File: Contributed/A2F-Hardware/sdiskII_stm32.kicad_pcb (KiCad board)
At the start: 2 copper layers, 71.1 x 124.5 mm, 59 parts, among them J1 SDISKII IN (CARD), J2 SDISKII OUT (DRIVE), J3 EA W128064-OLED (FPC31), J4 UART, U1 BlackPill STMF4X1, U2 DM-OLED096-636, U3 EA OLEDM128-6, U4 74x257

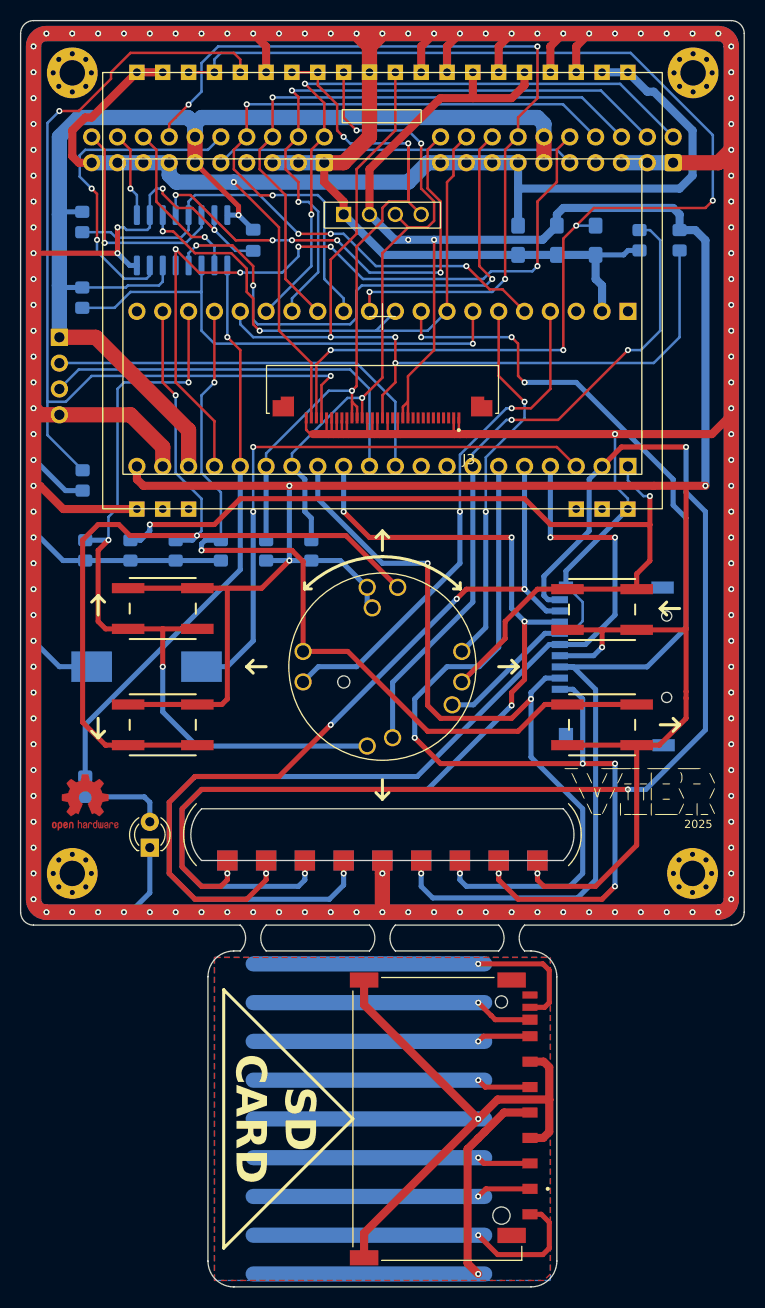
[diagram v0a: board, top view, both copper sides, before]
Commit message: Initial upload
Rotary encoder support buggy
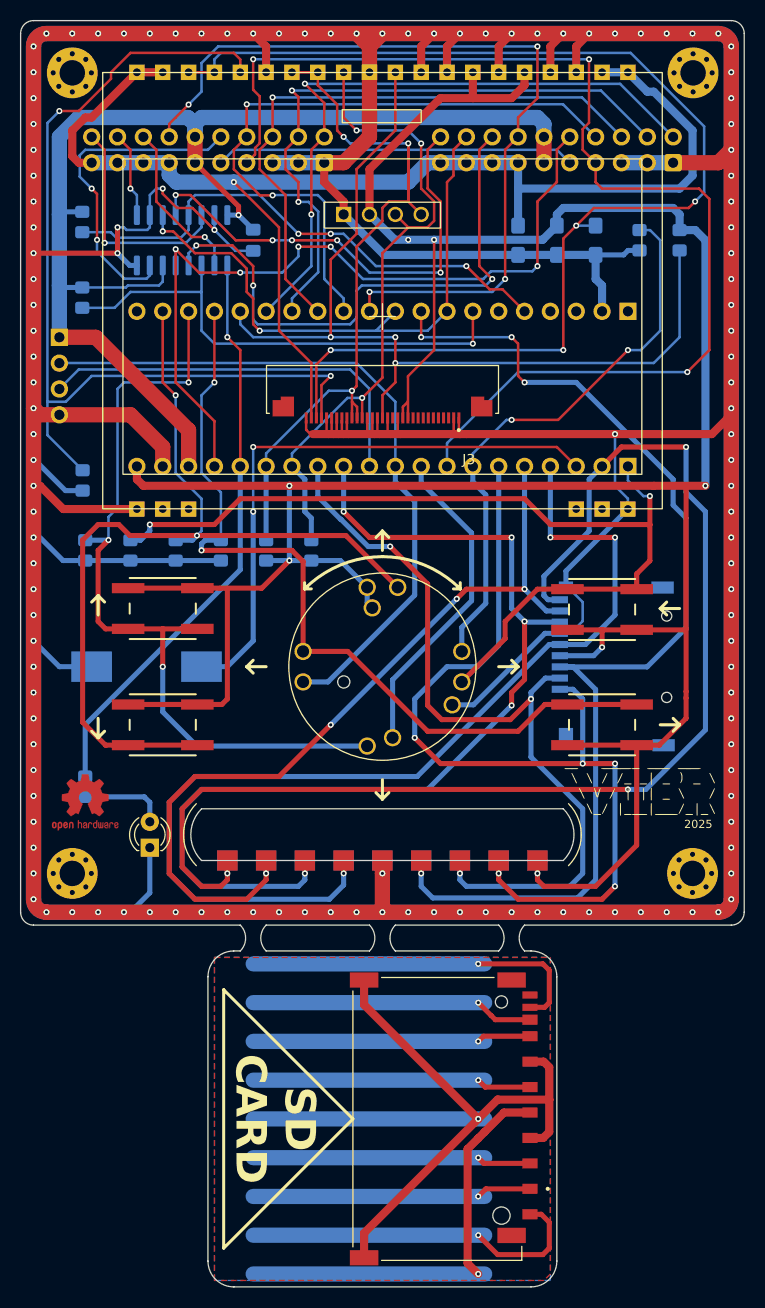
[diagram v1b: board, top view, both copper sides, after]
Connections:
- J1 pad 7: unconnected-(J1-Pin_7-Pad7) -> 3.5DSK
- J2 pad 7: unconnected-(J2-Pin_7-Pad7) -> 3.5DSK
- S5 pad EN_A: TIM2_CH3 -> USART1_TX
- S5 pad EN_B: TIM3_CH4 -> DEBUG
- S5 pad P: DEBUG -> USB_P
- U1 pad 8: unconnected-(U1-A11-Pad8) -> 3.5DSK
- U1 pad 9: unconnected-(U1-A12-Pad9) -> USB_P
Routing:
- net 3.5DSK: track 0.00 -> 115.4 mm, vias 0 -> 3
- net TIM2_CH3: track 50.1 -> 0.00 mm, vias 2 -> 0
- net TIM3_CH4: track 37.0 -> 0.00 mm, vias 2 -> 0
- net USB_P: track 0.00 -> 31.9 mm
- net USART1_TX: track 40.9 -> 68.9 mm
- net DEBUG: track 66.0 -> 55.7 mm
- net VCOMH: track 122.4 -> 120.7 mm
- net SDIO_D3: track 109.5 -> 108.3 mm

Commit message: RE update
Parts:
- added R13: 10K, Resistor_SMD:R_0805_2012Metric_Pad1.20x1.40mm_HandSolder, B.Cu at (151.1, 104.1)
- LS1: value BUZZER CT-1205H-SMT -> CT-1205H-SMT
- moved R12 35.5 mm to (146.7, 104.1)
- moved R2 4.19 mm to (164.7, 73.7)
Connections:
- R12 pad 1: DEBUG -> PA13
- S5 pad EN_A: USART1_TX -> PA13
- S5 pad EN_B: DEBUG -> PA14
- S5 pad P: USB_P -> unconnected-(S5A-PUSH-PadP)
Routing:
- net PA13: track 0.00 -> 57.3 mm, vias 0 -> 3
- net PA14: track 0.00 -> 56.5 mm, vias 0 -> 4
- net DEBUG: track 55.7 -> 0.00 mm, vias 2 -> 0
- net USB_P: track 31.9 -> 0.00 mm
- net USART1_TX: track 68.9 -> 44.1 mm
- net GND: track 425.7 -> 437.7 mm, vias 129 -> 131
- net BTN_DOWN: track 90.4 -> 97.0 mm
- net IREF: track 93.0 -> 97.7 mm
- net USART1_RX: track 39.7 -> 43.8 mm
- net BTN_UP: track 79.9 -> 82.7 mm
- net /RES: track 92.0 -> 89.5 mm
- net SDIO_D1: track 110.1 -> 111.9 mm
- net SDIO_D3: track 108.3 -> 109.9 mm
- net I2C_SCL: track 65.9 -> 67.3 mm
- net SDIO_D2: track 125.1 -> 126.3 mm
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
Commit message: Make Filsystem fixed
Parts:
- U1: footprint acheron_Hardware.pretty-master:Mini_F4X1_STM32_VIB -> sdisk_stm32:Mini_F4X1_STM32_VIB
- moved J4 1.27 mm to (108.0, 84.5)
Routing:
- net USART1_TX: track 44.1 -> 46.6 mm
- net USART1_RX: track 43.8 -> 46.0 mm
- net IREF: track 97.7 -> 99.3 mm
- net I2C_SCL: track 67.3 -> 68.3 mm
- net PA14: track 56.5 -> 55.7 mm, vias 4 -> 3
- net VCC: track 121.5 -> 120.8 mm
- net I2C_SDA: track 76.9 -> 77.5 mm
- net GND: track 437.7 -> 438.3 mm

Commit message: final v0.80.1
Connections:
- S5 pad P: unconnected-(S5A-PUSH-PadP) -> BTN_ENTR
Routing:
- net BTN_ENTR: track 82.4 -> 85.9 mm
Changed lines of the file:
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@@
 	(net 62 "unconnected-(U3-Pad3)")
 	(net 63 "unconnected-(SD2-WP-Pad11)")
-	(net 64 "unconnected-(S5A-PUSH-PadP)")
-	(net 65 "PA13")
-	(net 66 "PA14")
-	(net 67 "unconnected-(U1-3.3V-Pad41)")
-	(net 68 "unconnected-(U1-GND-Pad44)")
+	(net 64 "PA13")
+	(net 65 "PA14")
+	(net 66 "unconnected-(U1-3.3V-Pad41)")
+	(net 67 "unconnected-(U1-GND-Pad44)")
 	(footprint "sdisk_stm32:SD_CARD_AMPHENOL_GMC020080HR"
 		(layer "F.Cu")
@@
 			(layers "*.Cu" "*.Mask")
 			(remove_unused_layers no)
-			(net 65 "PA13")
+			(net 64 "PA13")
 			(pintype "passive")
 			(solder_mask_margin 0.102)
@@
 			(layers "*.Cu" "*.Mask")
 			(remove_unused_layers no)
-			(net 66 "PA14")
+			(net 65 "PA14")
 			(pintype "passive")
 			(solder_mask_margin 0.102)
@@
 			(layers "*.Cu" "*.Mask")
 			(remove_unused_layers no)
-			(net 64 "unconnected-(S5A-PUSH-PadP)")
+			(net 16 "BTN_ENTR")
 			(pinfunction "PUSH")
 			(pintype "passive")
@@
 			(layers "*.Cu" "*.Mask")
 			(remove_unused_layers no)
-			(net 67 "unconnected-(U1-3.3V-Pad41)")
+			(net 66 "unconnected-(U1-3.3V-Pad41)")
 			(pinfunction "3.3V")
 			(pintype "power_in+no_connect")
@@
 			(layers "*.Cu" "*.Mask")
 			(remove_unused_layers no)
-			(net 65 "PA13")
+			(net 64 "PA13")
 			(pinfunction "SDIO")
 			(pintype "bidirectional")
@@
 			(layers "*.Cu" "*.Mask")
 			(remove_unused_layers no)
-			(net 66 "PA14")
+			(net 65 "PA14")
 			(pinfunction "SCK")
 			(pintype "bidirectional")
@@
 			(layers "*.Cu" "*.Mask")
 			(remove_unused_layers no)
-			(net 68 "unconnected-(U1-GND-Pad44)")
+			(net 67 "unconnected-(U1-GND-Pad44)")
 			(pinfunction "GND")
 			(pintype "power_in+no_connect")
@@
 			(layers "B.Cu" "B.Mask" "B.Paste")
 			(roundrect_rratio 0.208333)
-			(net 65 "PA13")
+			(net 64 "PA13")
 			(pintype "passive")
 		)
@@
 			(layers "B.Cu" "B.Mask" "B.Paste")
 			(roundrect_rratio 0.208333)
-			(net 66 "PA14")
+			(net 65 "PA14")
 			(pintype "passive")
 		)
@@
 	)
 	(segment
-		(start 155.67 119.285)
-		(end 157.89 119.285)
+		(start 157.89 119.285)
+		(end 155.67 119.285)
 		(width 0.5)
 		(layer "F.Cu")
@@
 	)
 	(segment
-		(start 124.46 88.392)
-		(end 124.46 94.361)
-		(width 0.25)
+		(start 143.1102 120.142)
+		(end 143.129 120.142)
+		(width 0.5)
 		(layer "F.Cu")
 		(net 16)
 	)
 	(segment
-		(start 157.89 119.285)
-		(end 164.69 119.285)
+		(start 137.184 114.07)
+		(end 131.9022 114.07)
 		(width 0.5)
 		(layer "F.Cu")
@@
 	)
 	(segment
-		(start 131.9022 114.07)
-		(end 136.295 114.07)
+		(start 137.184 114.197)
+		(end 137.184 114.07)
 		(width 0.5)
 		(layer "F.Cu")
@@
 	)
 	(segment
-		(start 131.9022 105.2322)
-		(end 130.81 104.14)
+		(start 140.7022 122.55)
+		(end 143.1102 120.142)
 		(width 0.5)
 		(layer "F.Cu")
@@
 	)
 	(segment
-		(start 123.19 87.122)
-		(end 124.46 88.392)
+		(start 155.67 119.285)
+		(end 153.035 121.92)
+		(width 0.5)
+		(layer "F.Cu")
+		(net 16)
+	)
+	(segment
+		(start 124.46 88.392)
+		(end 124.46 94.361)
 		(width 0.25)
 		(layer "F.Cu")
@@
 	)
 	(segment
-		(start 136.295 114.07)
-		(end 144.145 121.92)
+		(start 143.129 120.142)
+		(end 137.184 114.197)
 		(width 0.5)
 		(layer "F.Cu")
@@
 	)
 	(segment
-		(start 144.145 121.92)
-		(end 153.035 121.92)
+		(start 157.89 119.285)
+		(end 164.69 119.285)
 		(width 0.5)
 		(layer "F.Cu")
@@
 	)
 	(segment
-		(start 153.035 121.92)
-		(end 155.67 119.285)
+		(start 131.9022 105.2322)
+		(end 130.81 104.14)
 		(width 0.5)
 		(layer "F.Cu")
@@
 	)
 	(segment
+		(start 123.19 87.122)
+		(end 124.46 88.392)
+		(width 0.25)
+		(layer "F.Cu")
+		(net 16)
+	)
+	(segment
 		(start 123.19 80.645)
 		(end 123.19 87.122)
@@
 	)
 	(segment
+		(start 144.907 121.92)
+		(end 143.129 120.142)
+		(width 0.5)
+		(layer "F.Cu")
+		(net 16)
+	)
+	(segment
 		(start 131.9022 114.07)
 		(end 131.9022 105.2322)
@@
 		(net 16)
 	)
+	(segment
+		(start 153.035 121.92)
+		(end 144.907 121.92)
+		(width 0.5)
+		(layer "F.Cu")
+		(net 16)
+	)
 	(via
 		(at 124.46 94.361)
@@
 		(width 0.25)
 		(layer "F.Cu")
-		(net 65)
+		(net 64)
 	)
 	(segment
@@
 		(width 0.25)
 		(layer "F.Cu")
-		(net 65)
+		(net 64)
 	)
 	(segment
@@
 		(width 0.25)
 		(layer "F.Cu")
-		(net 65)
+		(net 64)
 	)
 	(via
@@
 		(drill 0.3)
 		(layers "F.Cu" "B.Cu")
-		(net 65)
+		(net 64)
 	)
 	(via
@@
 		(drill 0.3)
 		(layers "F.Cu" "B.Cu")
-		(net 65)
+		(net 64)
 	)
 	(via
@@
 		(drill 0.3)
 		(layers "F.Cu" "B.Cu")
-		(net 65)
+		(net 64)
 	)
 	(segment
@@
 		(width 0.5)
 		(layer "B.Cu")
-		(net 65)
+		(net 64)
 	)
 	(segment
@@
 		(width 0.25)
 		(layer "B.Cu")
-		(net 65)
+		(net 64)
 	)
 	(segment
@@
 		(width 0.5)
 		(layer "B.Cu")
-		(net 65)
+		(net 64)
 	)
 	(segment
@@
 		(width 0.25)
 		(layer "B.Cu")
-		(net 65)
+		(net 64)
 	)
 	(segment
@@
 		(width 0.5)
 		(layer "B.Cu")
-		(net 65)
+		(net 64)
 	)
 	(segment
@@
 		(width 0.25)
 		(layer "B.Cu")
-		(net 65)
+		(net 64)
 	)
 	(segment
@@
 		(width 0.25)
 		(layer "B.Cu")
-		(net 65)
+		(net 64)
 	)
 	(segment
@@
 		(width 0.5)
 		(layer "B.Cu")
-		(net 65)
+		(net 64)
 	)
 	(segment
@@
 		(width 0.5)
 		(layer "B.Cu")
-		(net 65)
+		(net 64)
 	)
 	(segment
@@
 		(width 0.5)
 		(layer "B.Cu")
-		(net 65)
+		(net 64)
 	)
 	(segment
@@
 		(width 0.25)
 		(layer "B.Cu")
-		(net 65)
+		(net 64)
 	)
 	(segment
@@
 		(width 0.5)
 		(layer "B.Cu")
-		(net 65)
+		(net 64)
 	)
 	(segment
@@
 		(width 0.5)
 		(layer "B.Cu")
-		(net 65)
+		(net 64)
 	)
 	(segment
@@
 		(width 0.25)
 		(layer "F.Cu")
-		(net 66)
+		(net 65)
 	)
 	(segment
@@
 		(width 0.25)
 		(layer "F.Cu")
-		(net 66)
+		(net 65)
 	)
 	(segment
@@
 		(width 0.5)
 		(layer "F.Cu")
-		(net 66)
+		(net 65)
 	)
 	(segment
@@
 		(width 0.25)
 		(layer "F.Cu")
-		(net 66)
+		(net 65)
 	)
 	(segment
@@
 		(width 0.5)
 		(layer "F.Cu")
-		(net 66)
+		(net 65)
 	)
 	(via
@@
 		(drill 0.3)
 		(layers "F.Cu" "B.Cu")
-		(net 66)
+		(net 65)
 	)
 	(via
@@
 		(drill 0.3)
 		(layers "F.Cu" "B.Cu")
-		(net 66)
+		(net 65)
 	)
 	(via
@@
 		(drill 0.3)
 		(layers "F.Cu" "B.Cu")
-		(net 66)
+		(net 65)
 	)
 	(segment
@@
 		(width 0.25)
 		(layer "B.Cu")
-		(net 66)
+		(net 65)
 	)
 	(segment
@@
 		(width 0.25)
 		(layer "B.Cu")
-		(net 66)
+		(net 65)
 	)
 	(segment
@@
 		(width 0.25)
 		(layer "B.Cu")
-		(net 66)
+		(net 65)
 	)
 	(segment
@@
 		(width 0.25)
 		(layer "B.Cu")
-		(net 66)
+		(net 65)
 	)
 	(segment
@@
 		(width 0.25)
 		(layer "B.Cu")
-		(net 66)
+		(net 65)
 	)
 	(segment
@@
 		(width 0.5)
 		(layer "B.Cu")
-		(net 66)
+		(net 65)
 	)
 	(segment
@@
 		(width 0.5)
 		(layer "B.Cu")
-		(net 66)
+		(net 65)
 	)
 	(segment
@@
 		(width 0.25)
 		(layer "B.Cu")
-		(net 66)
+		(net 65)
 	)
 	(segment
@@
 		(width 0.25)
 		(layer "B.Cu")
-		(net 66)
+		(net 65)
 	)
 	(segment
@@
 		(width 0.25)
 		(layer "B.Cu")
-		(net 66)
+		(net 65)
 	)
 	(zone
